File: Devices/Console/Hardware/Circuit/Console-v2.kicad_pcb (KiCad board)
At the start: 2 copper layers, 96.8 x 62 mm, 31 parts, among them J1 AVR-ISP-6, J2 TYPE-C-31-M-12, J3 Conn_01x13, J4 Conn_01x04, J5 Conn_01x04, SW1 PEC11R-4220F-S0012, SW2 PEC11R-4220F-S0012, SW3 PEC11R-4220F-S0012, SW4 PEC11R-4220F-S0012, SW5 SW_Push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

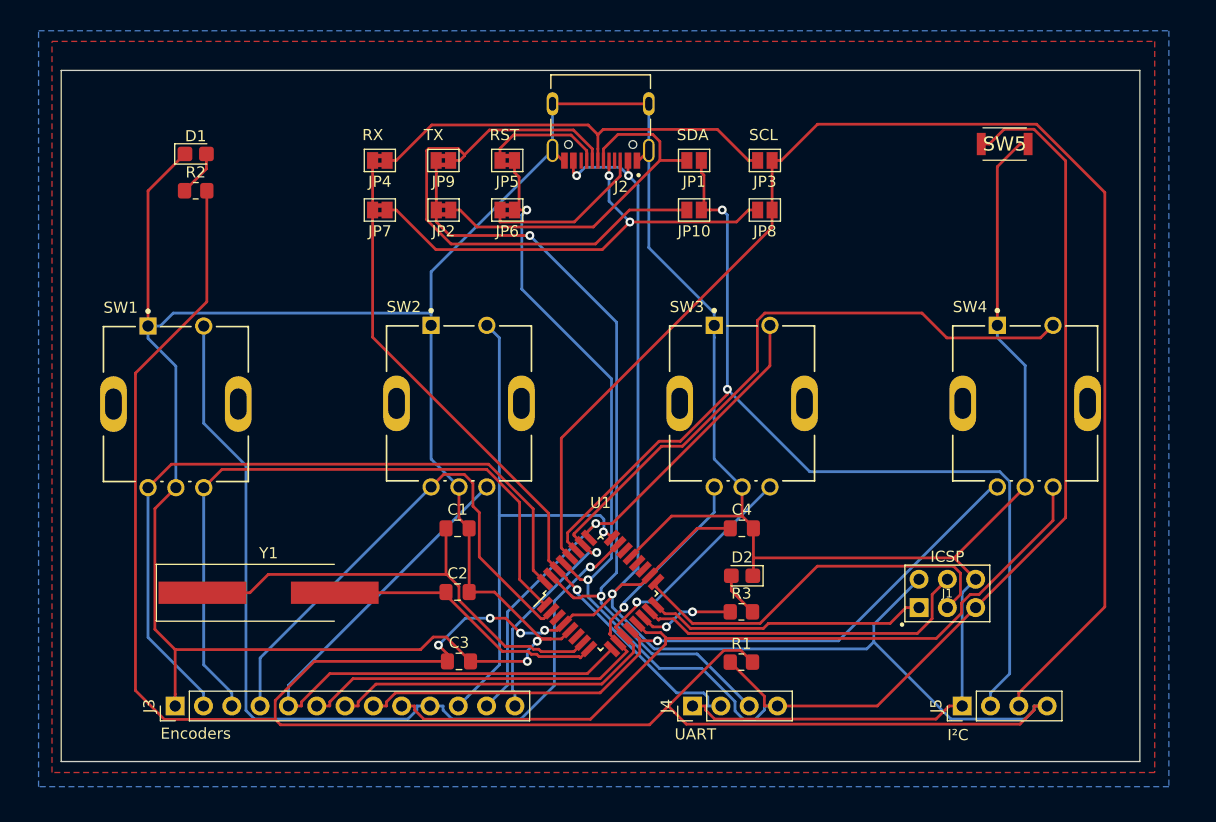
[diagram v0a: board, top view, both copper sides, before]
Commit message: Switch LED location
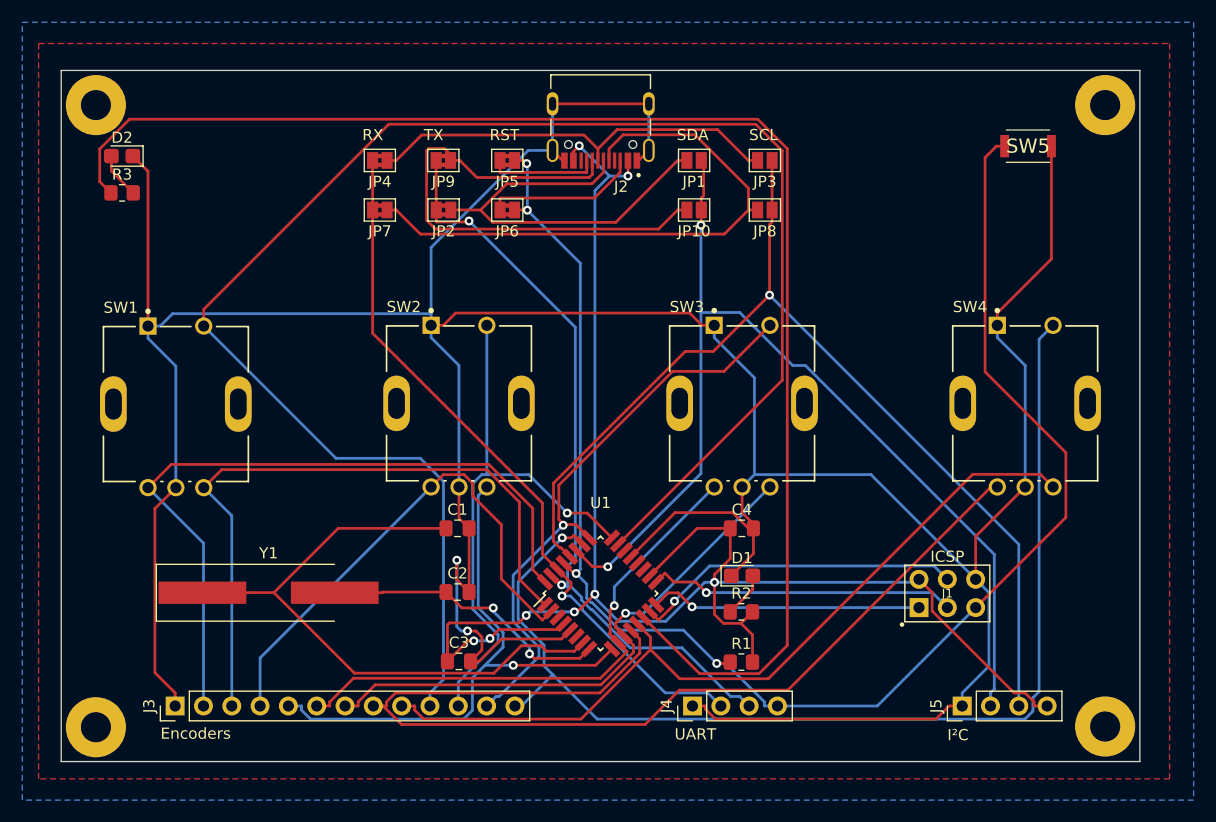
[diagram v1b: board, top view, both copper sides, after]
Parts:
- added PAD1: MountingHole_2.7mm_M2.5_Pad, MountingHole:MountingHole_2.7mm_M2.5_Pad, F.Cu at (101.0, 67.9)
- added PAD2: MountingHole_2.7mm_M2.5_Pad, MountingHole:MountingHole_2.7mm_M2.5_Pad, F.Cu at (191.5, 67.9)
- added PAD3: MountingHole_2.7mm_M2.5_Pad, MountingHole:MountingHole_2.7mm_M2.5_Pad, F.Cu at (101.0, 123.7)
- added PAD4: MountingHole_2.7mm_M2.5_Pad, MountingHole:MountingHole_2.7mm_M2.5_Pad, F.Cu at (191.5, 123.6)
- moved D2 67.2 mm to (103.3, 72.5)
- moved R3 67.1 mm to (103.3, 75.8)
- moved D1 61.9 mm to (158.9, 110.1)
- moved R2 61.8 mm to (158.9, 113.3)
- moved SW5 2.10 mm to (184.6, 71.6)
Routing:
- net VCC: track 295.0 -> 154.1 mm, vias 7 -> 8
- net LED: track 8.69 -> 128.8 mm, vias 2 -> 0
- net BTN1: track 82.1 -> 150.6 mm, vias 1 -> 0
- net SCL: track 126.7 -> 92.0 mm, vias 0 -> 1
- net BTN4: track 75.5 -> 102.4 mm
- net ENC4A: track 66.3 -> 93.1 mm, vias 1 -> 0
- net XTAL1: track 42.9 -> 56.5 mm
- net RST: track 151.0 -> 138.3 mm, vias 2 -> 4
- net Net-(J2-PadB7): track 42.5 -> 53.0 mm, vias 2 -> 0
- net SCK: track 35.1 -> 27.7 mm, vias 0 -> 1
- net ENC2B: track 58.4 -> 52.0 mm, vias 0 -> 1
- net GND: track 346.3 -> 340.6 mm
- net TX: track 73.7 -> 68.3 mm
- net BTN3: track 47.5 -> 52.6 mm
- net Net-(J2-PadA6): track 32.9 -> 37.4 mm
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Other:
- board text added: "20.08.2021"
- board text added: "Designed by: GHOSCHT"
- board text removed: "GHOSCHT - 2021"
